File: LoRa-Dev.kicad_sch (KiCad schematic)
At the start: 19 parts, among them J2 Barrel_Jack_MountingPin, J3 Conn_Coaxial_Small, U1 RPi Pico, U2 LT1963AEQ, U3 RFM95PW

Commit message: updated after first review
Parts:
- removed C4: 47uF, Capacitor_SMD:CP_Elec_6.3x5.8, symbol Device:C_Polarized_Small
- added C5: 47uf, Capacitor_SMD:C_1210_3225Metric, symbol Device:C_Small
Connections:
- net GND: now also C5.2; no longer U3.2 (GND)
- net RF_GND: now also U3.2 (GND)
- net RF_VDD: now also C5.1
- net DIO5: now reaches U1.20 (GP15)
- net DIO5: now also U3.15 (DIO5)
- net DIO2: now reaches U1.31 (GP26)
- net DIO2: now also U3.8 (DIO2)
- net DIO3: now reaches U1.32 (GP27)
- net DIO3: now also U3.3 (DIO3)
- net DIO4: now reaches U1.34 (GP28)
- net DIO4: now also U3.4 (DIO4)
- no-connect marks 5 -> 1
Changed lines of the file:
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@@
-	)
-	(no_connect
-		(at 233.68 57.15)
-	)
-	(no_connect
-		(at 187.96 62.23)
 	)
 	(no_connect
 		(at 222.25 72.39)
 	)
-	(no_connect
-		(at 187.96 72.39)
-	)
-	(no_connect
-		(at 187.96 59.69)
-	)
 	(wire
 		(pts
@@
 	(wire
 		(pts
+			(xy 76.2 71.12) (xy 87.63 71.12)
+		)
+		(stroke
+			(width 0)
+			(type default)
+		)
+	)
+	(wire
+		(pts
 			(xy 91.44 138.43) (xy 91.44 135.89)
 		)
@@
 	(wire
 		(pts
+			(xy 45.72 96.52) (xy 34.29 96.52)
+		)
+		(stroke
+			(width 0)
+			(type default)
+		)
+	)
+	(wire
+		(pts
 			(xy 83.82 135.89) (xy 91.44 135.89)
 		)
@@
 	(wire
 		(pts
+			(xy 76.2 68.58) (xy 87.63 68.58)
+		)
+		(stroke
+			(width 0)
+			(type default)
+		)
+	)
+	(wire
+		(pts
 			(xy 73.66 135.89) (xy 73.66 140.97)
 		)
@@
 		(pts
 			(xy 157.48 64.77) (xy 157.48 68.58)
+		)
+		(stroke
+			(width 0)
+			(type default)
+		)
+	)
+	(wire
+		(pts
+			(xy 76.2 63.5) (xy 87.63 63.5)
 		)
 		(stroke
@@
 		)
 	)
+	(label "DIO2"
+		(at 189.23 72.39 0)
+		(fields_autoplaced yes)
+		(effects
+			(font
+				(size 1.27 1.27)
+			)
+			(justify left bottom)
+		)
+	)
+	(label "DIO3"
+		(at 78.74 68.58 0)
+		(fields_autoplaced yes)
+		(effects
+			(font
+				(size 1.27 1.27)
+			)
+			(justify left bottom)
+		)
+	)
 	(label "DIO1"
 		(at 78.74 81.28 0)
@@
 		)
 	)
+	(label "DIO5"
+		(at 223.52 57.15 0)
+		(fields_autoplaced yes)
+		(effects
+			(font
+				(size 1.27 1.27)
+			)
+			(justify left bottom)
+		)
+	)
 	(label "DIO1"
 		(at 189.23 69.85 0)
@@
 		)
 	)
+	(label "DIO3"
+		(at 189.23 59.69 0)
+		(fields_autoplaced yes)
+		(effects
+			(font
+				(size 1.27 1.27)
+			)
+			(justify left bottom)
+		)
+	)
 	(label "RF_GND"
 		(at 240.03 39.37 0)
@@
 		)
 	)
+	(label "DIO2"
+		(at 78.74 71.12 0)
+		(fields_autoplaced yes)
+		(effects
+			(font
+				(size 1.27 1.27)
+			)
+			(justify left bottom)
+		)
+	)
 	(label "GND"
 		(at 78.74 91.44 0)
@@
 		)
 	)
+	(label "DIO4"
+		(at 189.23 62.23 0)
+		(fields_autoplaced yes)
+		(effects
+			(font
+				(size 1.27 1.27)
+			)
+			(justify left bottom)
+		)
+	)
 	(label "DIO0"
 		(at 189.23 67.31 0)
@@
 		)
 	)
+	(label "DIO5"
+		(at 43.18 96.52 180)
+		(fields_autoplaced yes)
+		(effects
+			(font
+				(size 1.27 1.27)
+			)
+			(justify right bottom)
+		)
+	)
 	(label "DIO0"
 		(at 78.74 83.82 0)
@@
 		)
 	)
-	(label "GND"
+	(label "DIO4"
+		(at 78.74 63.5 0)
+		(fields_autoplaced yes)
+		(effects
+			(font
+				(size 1.27 1.27)
+			)
+			(justify left bottom)
+		)
+	)
+	(label "RF_GND"
 		(at 189.23 57.15 0)
 		(fields_autoplaced yes)
@@
 	)
 	(symbol
+		(lib_id "Device:C_Small")
+		(at 157.48 71.12 0)
+		(unit 1)
+		(exclude_from_sim no)
+		(in_bom yes)
+		(on_board yes)
+		(dnp no)
+		(fields_autoplaced yes)
+		(property "Reference" "C5"
+			(at 160.02 69.8562 0)
+			(effects
+				(font
+					(size 1.27 1.27)
+				)
+				(justify left)
+			)
+		)
+		(property "Value" "47uf"
+			(at 160.02 72.3962 0)
+			(effects
+				(font
+					(size 1.27 1.27)
+				)
+				(justify left)
+			)
+		)
+		(property "Footprint" "Capacitor_SMD:C_1210_3225Metric"
+			(at 157.48 71.12 0)
+			(effects
+				(font
+					(size 1.27 1.27)
+				)
+				(hide yes)
+			)
+		)
+		(property "Datasheet" "~"
+			(at 157.48 71.12 0)
+			(effects
+				(font
+					(size 1.27 1.27)
+				)
+				(hide yes)
+			)
+		)
+		(property "Description" "Unpolarized capacitor, small symbol"
+			(at 157.48 71.12 0)
+			(effects
+				(font
+					(size 1.27 1.27)
+				)
+				(hide yes)
+			)
+		)
+		(pin "2"
+		)
+		(pin "1"
+		)
+		(instances
+			(project "LoRa-Dev"
+				(path "/ef1cdc4e-4ca4-4643-8589-6d5225afae9e"
+					(reference "C5")
+					(unit 1)
+				)
+			)
+		)
+	)
+	(symbol
 		(lib_id "Regulator_Linear:LT1963AEQ")
 		(at 104.14 138.43 0)
@@
 					(unit 1)
 				)
-			)
-		)
-	)
-	(symbol
-		(lib_id "Device:C_Polarized_Small")
-		(at 157.48 71.12 0)
-		(unit 1)
-		(exclude_from_sim no)
-		(in_bom yes)
-		(on_board yes)
-		(dnp no)
-		(fields_autoplaced yes)
-		(property "Reference" "C4"
-			(at 160.02 69.3038 0)
-			(effects
-				(font
-					(size 1.27 1.27)
-				)
-				(justify left)
-			)
-		)
-		(property "Value" "47uF"
-			(at 160.02 71.8438 0)
-			(effects
-				(font
-					(size 1.27 1.27)
-				)
-				(justify left)
-			)
-		)
-		(property "Footprint" "Capacitor_SMD:CP_Elec_6.3x5.8"
-			(at 157.48 71.12 0)
-			(effects
-				(font
-					(size 1.27 1.27)
-				)
-				(hide yes)
-			)
-		)
-		(property "Datasheet" "~"
-			(at 157.48 71.12 0)
-			(effects
-				(font
-					(size 1.27 1.27)
-				)
-				(hide yes)
-			)
-		)
-		(property "Description" "Polarized capacitor, small symbol"
-			(at 157.48 71.12 0)
-			(effects
-				(font
-					(size 1.27 1.27)
-				)
-				(hide yes)
-			)
-		)
-		(pin "1"
-		)
-		(pin "2"
-		)
-		(instances
-			(project "LoRa-Dev"
-				(path "/ef1cdc4e-4ca4-4643-8589-6d5225afae9e"
-					(reference "C4")
-					(unit 1)
-				)

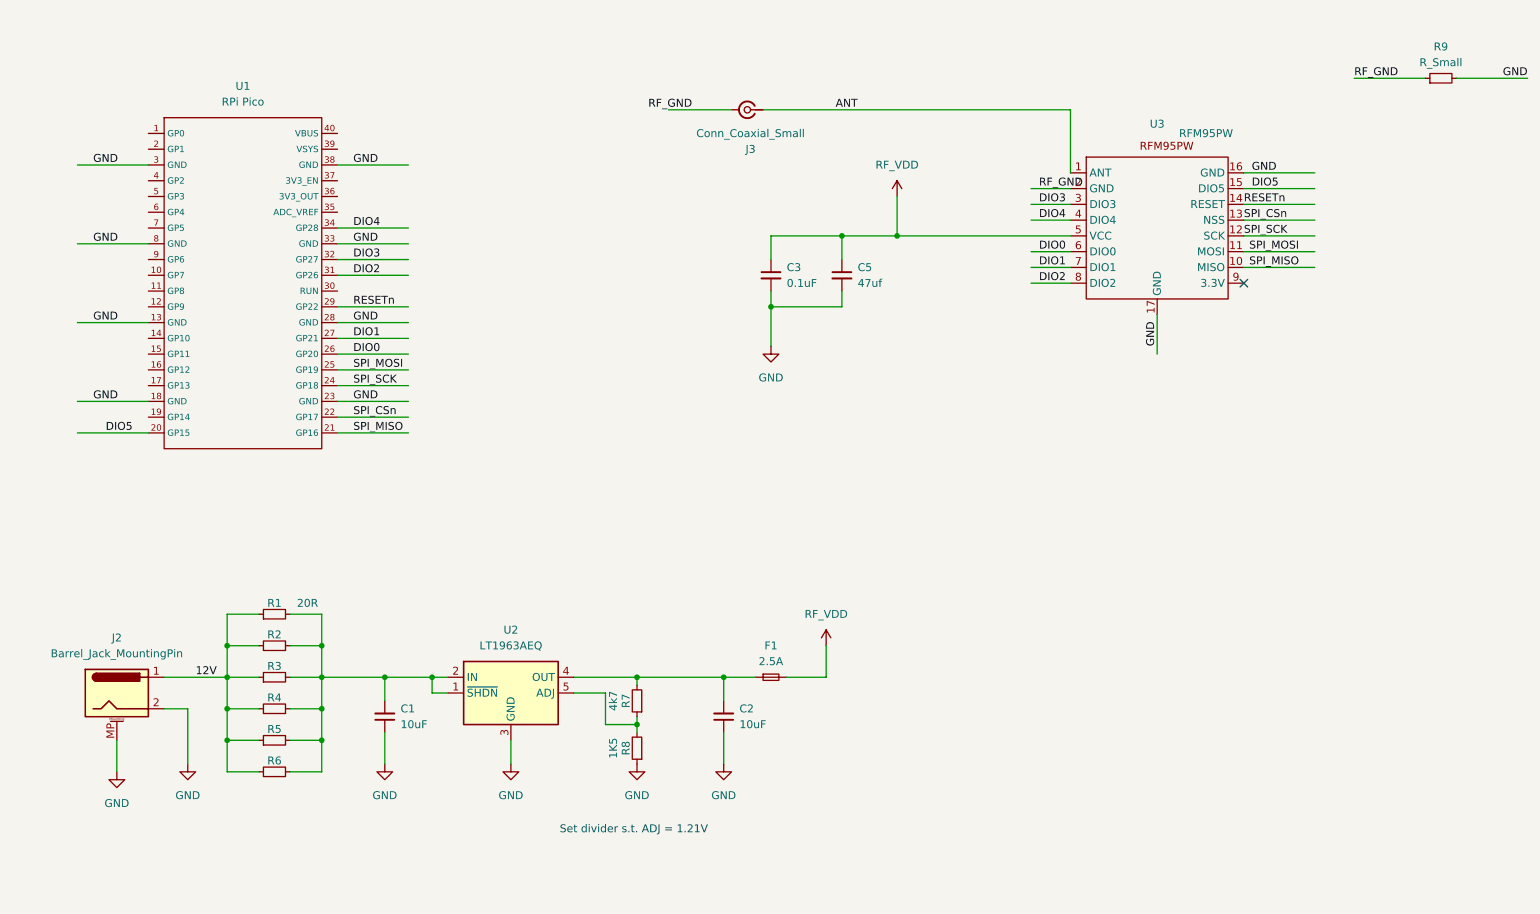
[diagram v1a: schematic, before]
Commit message: Minor fixes, exported BOM
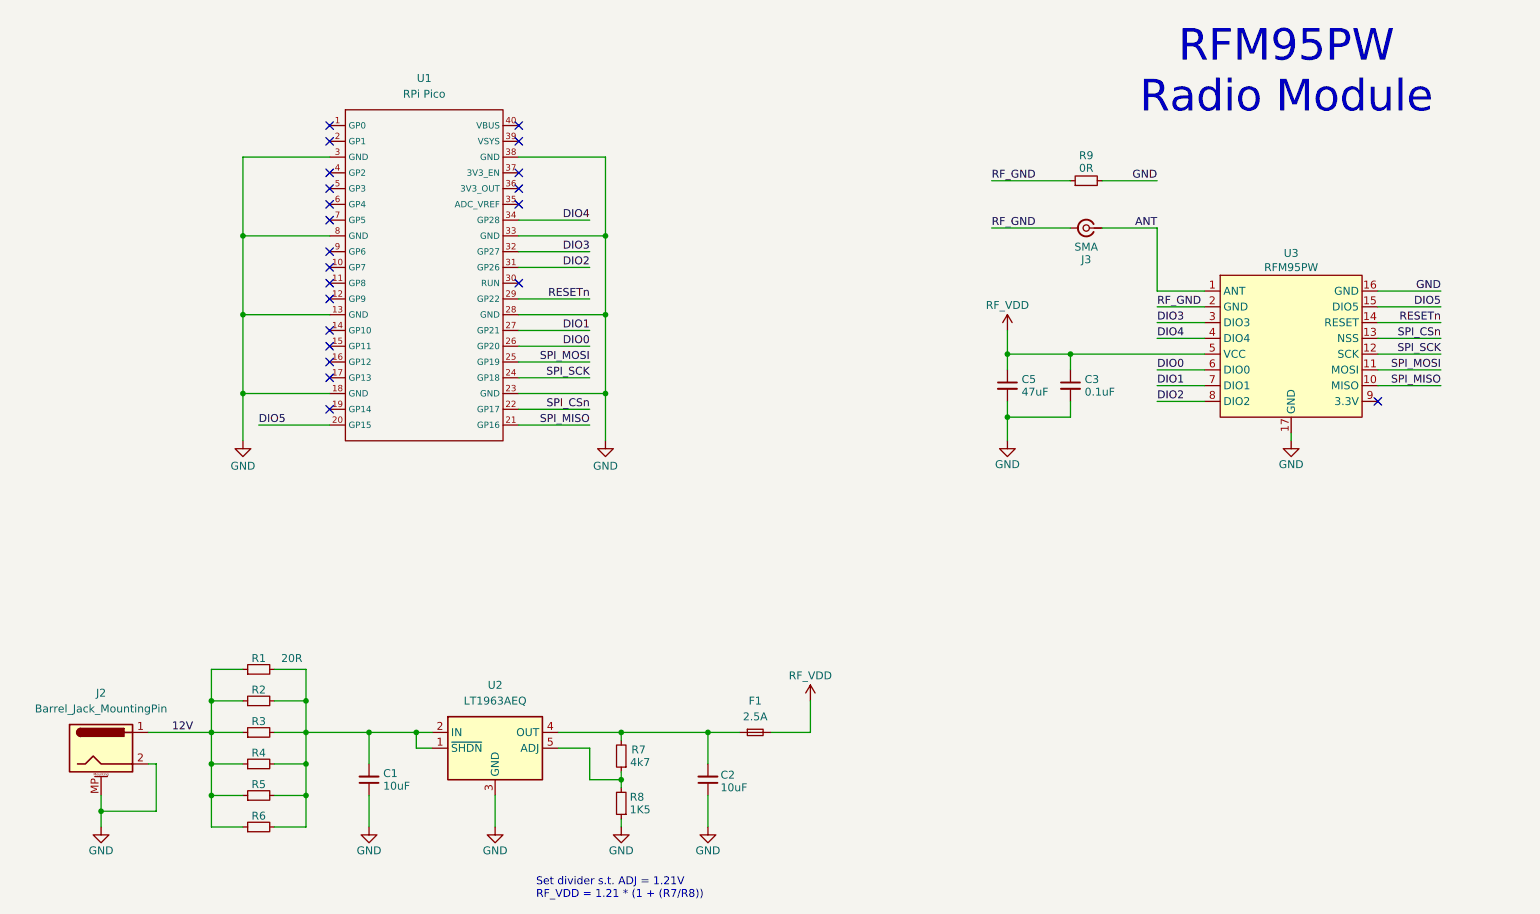
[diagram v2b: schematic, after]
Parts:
- C5: value 47uf -> 47uF
- J3: value Conn_Coaxial_Small -> SMA; footprint Connector_Coaxial:U.FL_Hirose_U.FL-R-SMT-1_Vertical -> Connector_Coaxial:SMA_Amphenol_901-144_Vertical
- R9: value R_Small -> 0R
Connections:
- no-connect marks 1 -> 22
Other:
- note added: "RFM95PW Radio Module"
- note added: "Set divider s.t. ADJ = 1.21V RF_VDD = 1.21 * (1 + (R7/R8))"
- note removed: "Set divider s.t. ADJ = 1.21V"
- moved on the sheet: C1, C2, C3, C5, F1, J2, J3, R1, R2, R3, R4, R5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
